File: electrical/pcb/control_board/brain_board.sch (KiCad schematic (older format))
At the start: 7 parts, among them J10 6posheader, J27 PPTC102LFBN-RC, J6 S9175-ND_rpi_breakout, J7 S9175-ND_rpi_breakout, J8 6posheader

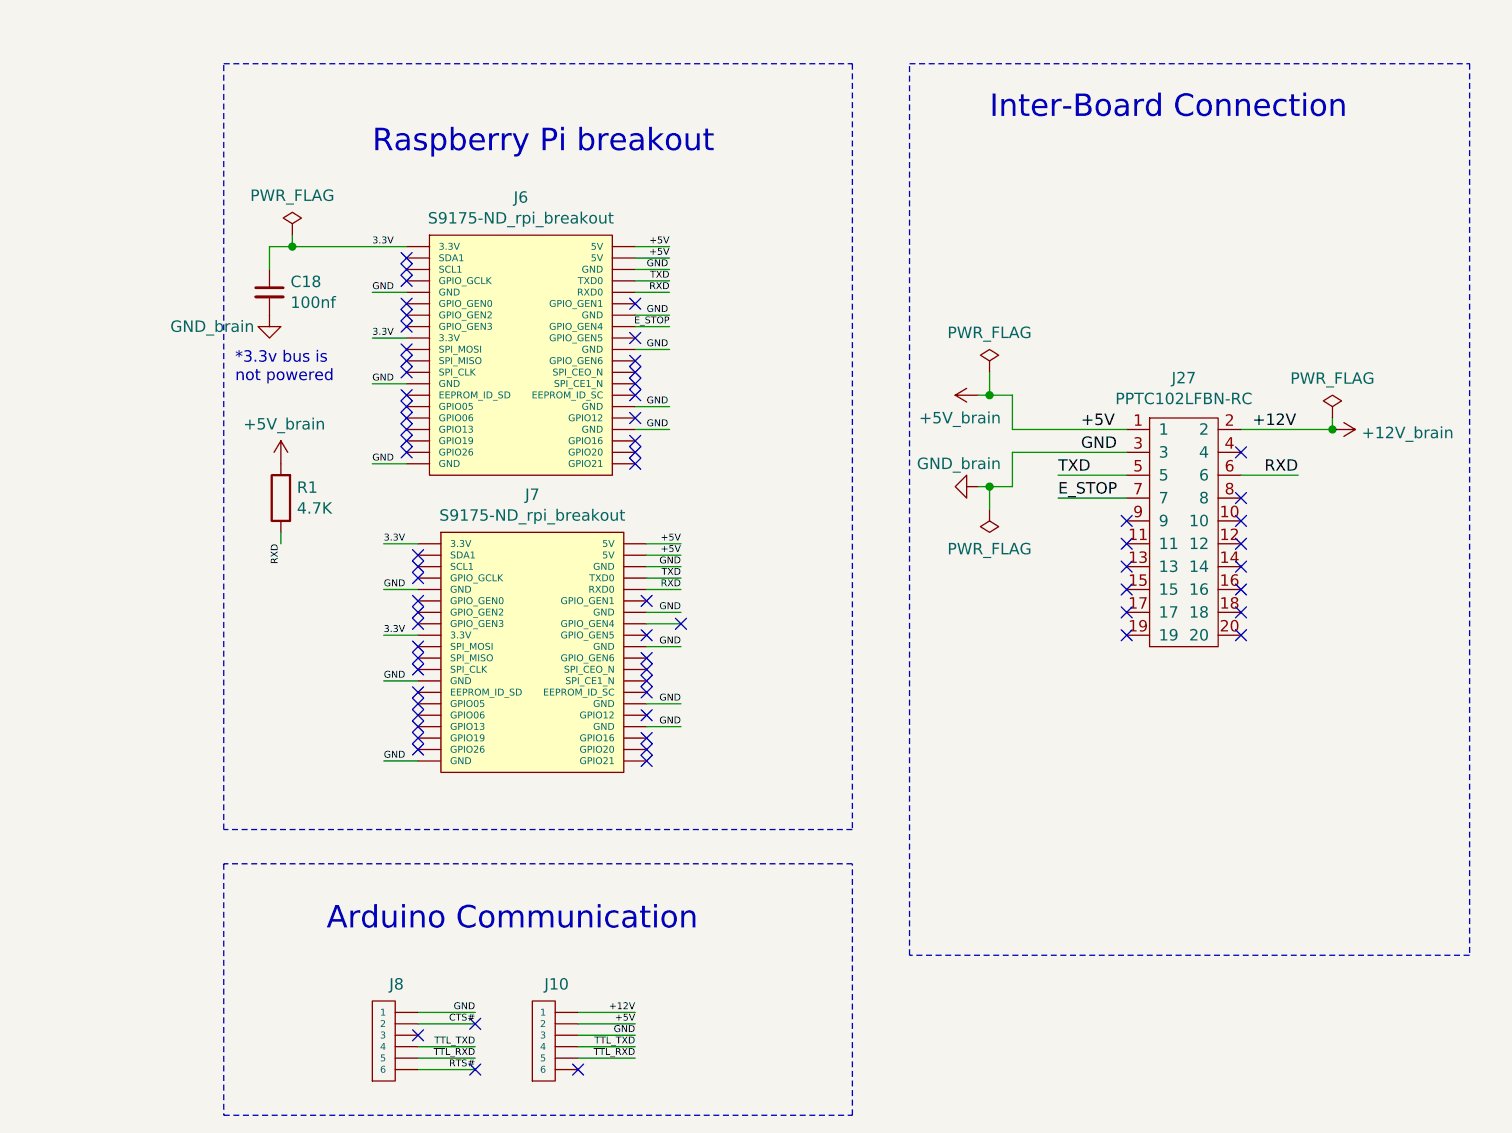
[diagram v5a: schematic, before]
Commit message: Adding secondary e-stop line connected to s4 on roboclaw, along with a 2 pin header for it on the brain board
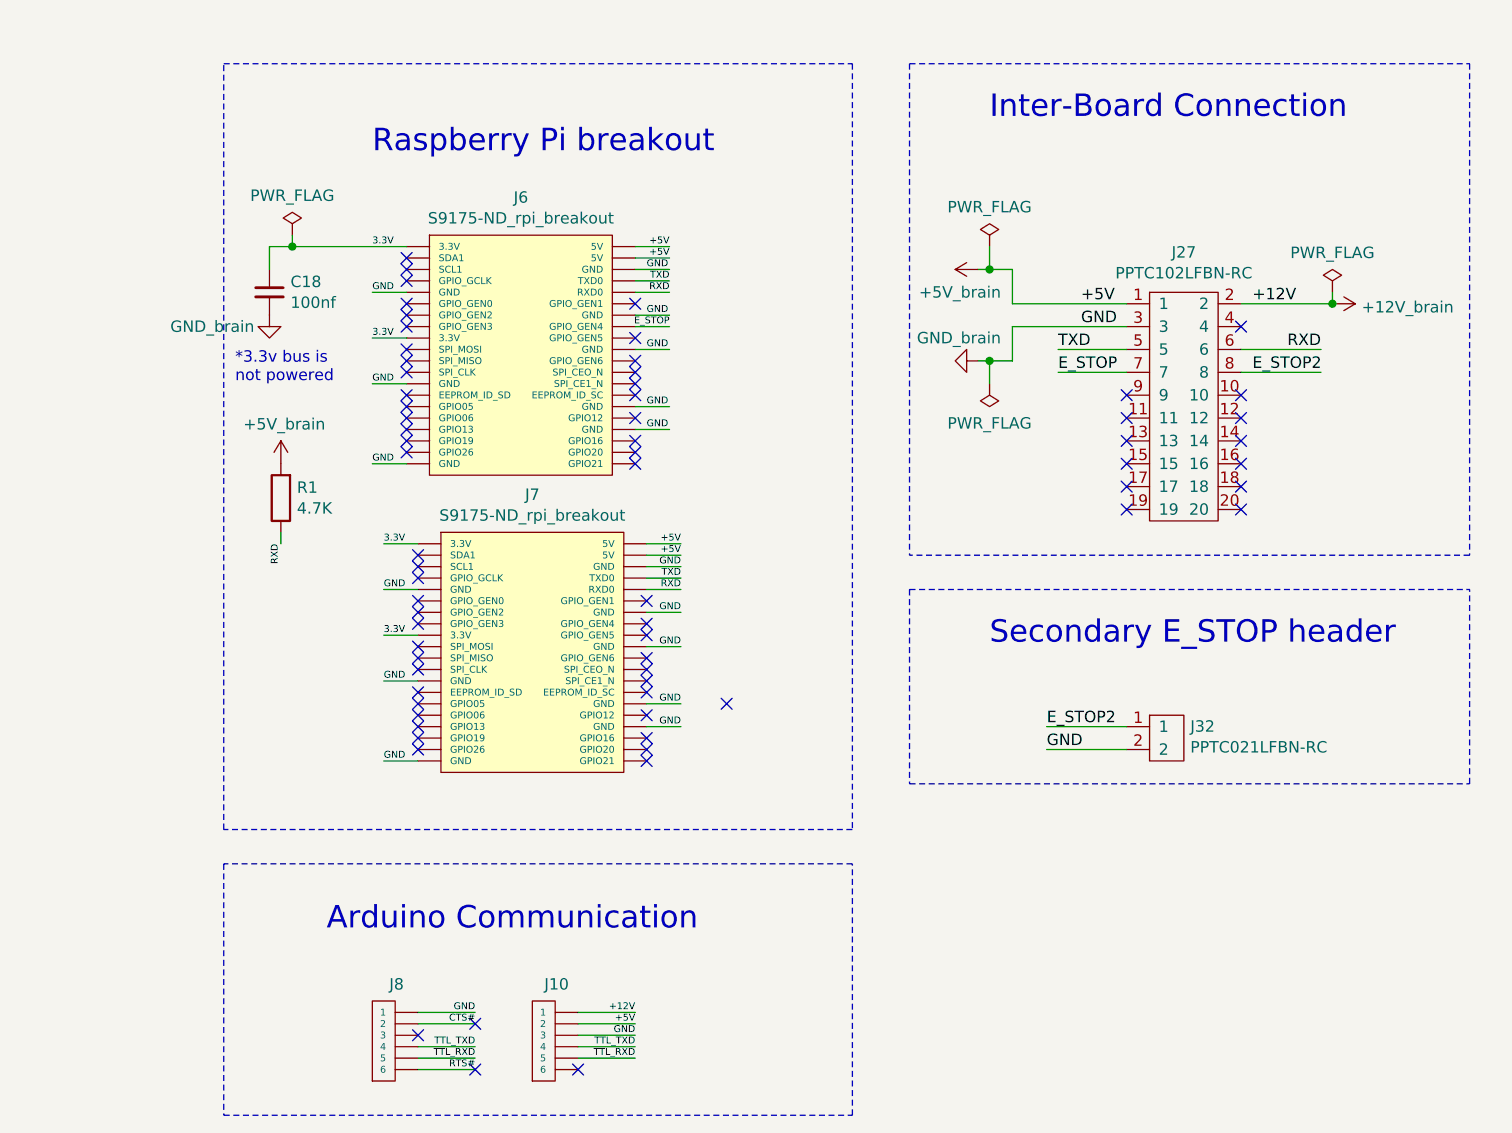
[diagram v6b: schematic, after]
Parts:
- added J32: PPTC021LFBN-RC, JPL Robotics:PPTC021LFBN-RC, symbol JPL_Robotics_Lib:PPTC021LFBN-RC
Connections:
- net labels added: E_STOP2
- wire segments 59 -> 61
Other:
- note added: "Secondary E_STOP header"
- moved on the sheet: J27
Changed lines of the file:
@@
 Wire Wire Line
 	4550 5700 4800 5700
-Wire Wire Line
-	5000 3850 4850 3850
 NoConn ~ 4550 5800
 NoConn ~ 4100 5800
 NoConn ~ 4100 5600
-NoConn ~ 5000 3850
 NoConn ~ 3800 2650
 NoConn ~ 3800 2750
@@
 NoConn ~ 3850 3600
 Wire Notes Line style solid rgb(0, 0, 0)
-	8450 1400 8450 5300
-Wire Notes Line style solid rgb(0, 0, 0)
-	8450 5300 6000 5300
-Wire Notes Line style solid rgb(0, 0, 0)
-	6000 5300 6000 1400
-Wire Notes Line style solid rgb(0, 0, 0)
 	6000 1400 8450 1400
 Text Notes 6350 1650 0    98   ~ 0
 Inter-Board Connection
-Text Label 6650 3200 0    50   ~ 0
+Text Label 6650 2650 0    50   ~ 0
 TXD
-Text Label 7700 3200 2    50   ~ 0
+Text Label 7800 2650 2    50   ~ 0
 RXD
-Text Label 6650 3300 0    50   ~ 0
+Text Label 6650 2750 0    50   ~ 0
 E_STOP
 Wire Wire Line
-	6650 3200 6950 3200
-Wire Wire Line
-	6650 3300 6950 3300
-Wire Wire Line
-	7450 3200 7700 3200
+	6650 2650 6950 2650
+Wire Wire Line
+	6650 2750 6950 2750
 $Comp
 L JPL_Robotics_Lib:PPTC102LFBN-RC J27
 U 1 1 60EE139B
-P 7200 2850
-F 0 "J27" H 7200 2925 50  0000 C CNN
-F 1 "PPTC102LFBN-RC" H 7200 2834 50  0000 C CNN
-F 2 "JPL Robotics:PPTC102LFBN-RC" H 7500 2850 50  0001 C CNN
-F 3 "" H 7500 2850 50  0001 C CNN
-	1    7200 2850
-	1    0    0    -1
-$EndComp
-NoConn ~ 7450 3300
-NoConn ~ 7450 3400
-NoConn ~ 7450 3500
-NoConn ~ 7450 3600
-NoConn ~ 7450 3700
-NoConn ~ 7450 3800
-NoConn ~ 7450 3900
-NoConn ~ 6950 3400
-NoConn ~ 6950 3500
-NoConn ~ 6950 3600
-NoConn ~ 6950 3700
-NoConn ~ 6950 3800
-NoConn ~ 6950 3900
+P 7200 2300
+F 0 "J27" H 7200 2375 50  0000 C CNN
+F 1 "PPTC102LFBN-RC" H 7200 2284 50  0000 C CNN
+F 2 "JPL Robotics:PPTC102LFBN-RC" H 7500 2300 50  0001 C CNN
+F 3 "" H 7500 2300 50  0001 C CNN
+	1    7200 2300
+	1    0    0    -1
+$EndComp
+NoConn ~ 7450 2850
+NoConn ~ 7450 2950
+NoConn ~ 7450 3050
+NoConn ~ 7450 3150
+NoConn ~ 7450 3250
+NoConn ~ 7450 3350
+NoConn ~ 6950 2850
+NoConn ~ 6950 2950
+NoConn ~ 6950 3050
+NoConn ~ 6950 3150
+NoConn ~ 6950 3250
+NoConn ~ 6950 3350
 $Comp
 L JPL_Robotics_Lib:+5V_brain #PWR0144
@@
 L JPL_Robotics_Lib:+5V_brain #PWR0146
 U 1 1 618ECDE5
-P 6300 2850
-F 0 "#PWR0146" H 6300 2700 50  0001 C CNN
-F 1 "+5V_brain" V 6200 2750 50  0000 L CNN
-F 2 "" H 6300 2850 50  0001 C CNN
-F 3 "" H 6300 2850 50  0001 C CNN
-	1    6300 2850
+P 6300 2300
+F 0 "#PWR0146" H 6300 2150 50  0001 C CNN
+F 1 "+5V_brain" V 6200 2200 50  0000 L CNN
+F 2 "" H 6300 2300 50  0001 C CNN
+F 3 "" H 6300 2300 50  0001 C CNN
+	1    6300 2300
 	0    -1   -1   0
 $EndComp
@@
 L JPL_Robotics_Lib:GND_brain #PWR0147
 U 1 1 618EE99B
-P 6300 3250
-F 0 "#PWR0147" H 6300 3000 50  0001 C CNN
-F 1 "GND_brain" V 6200 3350 50  0000 R CNN
-F 2 "" H 6300 3250 50  0001 C CNN
-F 3 "" H 6300 3250 50  0001 C CNN
-	1    6300 3250
+P 6300 2700
+F 0 "#PWR0147" H 6300 2450 50  0001 C CNN
+F 1 "GND_brain" V 6200 2800 50  0000 R CNN
+F 2 "" H 6300 2700 50  0001 C CNN
+F 3 "" H 6300 2700 50  0001 C CNN
+	1    6300 2700
 	0    1    1    0
 $EndComp
@@
 L JPL_Robotics_Lib:+12V_brain #PWR0148
 U 1 1 618F0639
-P 7850 3000
-F 0 "#PWR0148" H 7850 2850 50  0001 C CNN
-F 1 "+12V_brain" V 7865 3128 50  0000 L CNN
-F 2 "" H 7850 3000 50  0001 C CNN
-F 3 "" H 7850 3000 50  0001 C CNN
-	1    7850 3000
+P 7850 2450
+F 0 "#PWR0148" H 7850 2300 50  0001 C CNN
+F 1 "+12V_brain" V 7865 2578 50  0000 L CNN
+F 2 "" H 7850 2450 50  0001 C CNN
+F 3 "" H 7850 2450 50  0001 C CNN
+	1    7850 2450
 	0    1    1    0
 $EndComp
-Text Label 6750 3000 0    50   ~ 0
+Text Label 6750 2450 0    50   ~ 0
 +5V
-Text Label 6750 3100 0    50   ~ 0
+Text Label 6750 2550 0    50   ~ 0
 GND
-Text Label 7500 3000 0    50   ~ 0
+Text Label 7500 2450 0    50   ~ 0
 +12V
-NoConn ~ 7450 3100
+NoConn ~ 7450 2550
 $Comp
 L power:PWR_FLAG #FLG0101
 U 1 1 6195B322
-P 6350 2750
-F 0 "#FLG0101" H 6350 2825 50  0001 C CNN
-F 1 "PWR_FLAG" H 6350 2923 50  0000 C CNN
-F 2 "" H 6350 2750 50  0001 C CNN
-F 3 "~" H 6350 2750 50  0001 C CNN
-	1    6350 2750
+P 6350 2200
+F 0 "#FLG0101" H 6350 2275 50  0001 C CNN
+F 1 "PWR_FLAG" H 6350 2373 50  0000 C CNN
+F 2 "" H 6350 2200 50  0001 C CNN
+F 3 "~" H 6350 2200 50  0001 C CNN
+	1    6350 2200
 	1    0    0    -1
 $EndComp
@@
 L power:PWR_FLAG #FLG0102
 U 1 1 6195CC58
-P 6350 3350
-F 0 "#FLG0102" H 6350 3425 50  0001 C CNN
-F 1 "PWR_FLAG" H 6350 3523 50  0000 C CNN
-F 2 "" H 6350 3350 50  0001 C CNN
-F 3 "~" H 6350 3350 50  0001 C CNN
-	1    6350 3350
+P 6350 2800
+F 0 "#FLG0102" H 6350 2875 50  0001 C CNN
+F 1 "PWR_FLAG" H 6350 2973 50  0000 C CNN
+F 2 "" H 6350 2800 50  0001 C CNN
+F 3 "~" H 6350 2800 50  0001 C CNN
+	1    6350 2800
 	-1   0    0    1
 $EndComp
 Wire Wire Line
-	6450 3250 6350 3250
-Wire Wire Line
-	6450 3100 6950 3100
-Wire Wire Line
-	6350 3250 6350 3350
-Connection ~ 6350 3250
-Wire Wire Line
-	6350 3250 6300 3250
-Wire Wire Line
-	6450 2850 6350 2850
-Wire Wire Line
-	6450 3000 6950 3000
-Wire Wire Line
-	6350 2850 6350 2750
-Connection ~ 6350 2850
-Wire Wire Line
-	6350 2850 6300 2850
-Wire Wire Line
-	6450 3100 6450 3250
-Wire Wire Line
-	6450 2850 6450 3000
-Wire Wire Line
-	7450 3000 7850 3000
+	6450 2700 6350 2700
+Wire Wire Line
+	6450 2550 6950 2550
+Wire Wire Line
+	6350 2700 6350 2800
+Connection ~ 6350 2700
+Wire Wire Line
+	6350 2700 6300 2700
+Wire Wire Line
+	6450 2300 6350 2300
+Wire Wire Line
+	6450 2450 6950 2450
+Wire Wire Line
+	6350 2300 6350 2200
+Connection ~ 6350 2300
+Wire Wire Line
+	6350 2300 6300 2300
+Wire Wire Line
+	6450 2550 6450 2700
+Wire Wire Line
+	6450 2300 6450 2450
+Wire Wire Line
+	7450 2450 7850 2450
 $Comp
 L power:PWR_FLAG #FLG0103
 U 1 1 619765A5
-P 7850 2950
-F 0 "#FLG0103" H 7850 3025 50  0001 C CNN
-F 1 "PWR_FLAG" H 7850 3123 50  0000 C CNN
-F 2 "" H 7850 2950 50  0001 C CNN
-F 3 "~" H 7850 2950 50  0001 C CNN
-	1    7850 2950
-	1    0    0    -1
-$EndComp
-Wire Wire Line
-	7850 2950 7850 3000
-Connection ~ 7850 3000
+P 7850 2400
+F 0 "#FLG0103" H 7850 2475 50  0001 C CNN
+F 1 "PWR_FLAG" H 7850 2573 50  0000 C CNN
+F 2 "" H 7850 2400 50  0001 C CNN
+F 3 "~" H 7850 2400 50  0001 C CNN
+	1    7850 2400
+	1    0    0    -1
+$EndComp
+Wire Wire Line
+	7850 2400 7850 2450
+Connection ~ 7850 2450
+NoConn ~ 4850 3850
+NoConn ~ 5200 4200
+Wire Notes Line
+	6000 1400 6000 3550
+Wire Notes Line
+	8450 1400 8450 3550
+Wire Notes Line
+	8450 3550 6000 3550
+Wire Notes Line style solid rgb(0, 0, 0)
+	6000 3700 8450 3700
+Text Notes 6350 3950 0    98   ~ 0
+Secondary E_STOP header
+$Comp
+L JPL_Robotics_Lib:PPTC021LFBN-RC J32
+U 1 1 609D84ED
+P 7200 4150
+F 0 "J32" H 7228 4001 50  0000 L CNN
+F 1 "PPTC021LFBN-RC" H 7228 3910 50  0000 L CNN
+F 2 "JPL Robotics:PPTC021LFBN-RC" H 7500 4150 50  0001 C CNN
+F 3 "" H 7500 4150 50  0001 C CNN
+	1    7200 4150
+	1    0    0    -1
+$EndComp
+Wire Wire Line
+	7450 2750 7800 2750
+Text Label 7500 2750 0    50   ~ 0
+E_STOP2
+Wire Wire Line
+	7450 2650 7800 2650
+Wire Wire Line
+	6600 4400 6950 4400
+Wire Wire Line
+	6600 4300 6950 4300
+Text Label 6600 4300 0    50   ~ 0
+E_STOP2
+Text Label 6600 4400 0    50   ~ 0
+GND
+Wire Notes Line
+	6000 3700 6000 4550
+Wire Notes Line
+	6000 4550 8450 4550
+Wire Notes Line
+	8450 4550 8450 3700
 $EndSCHEMATC

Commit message: Adding headers and rpi connections for gst
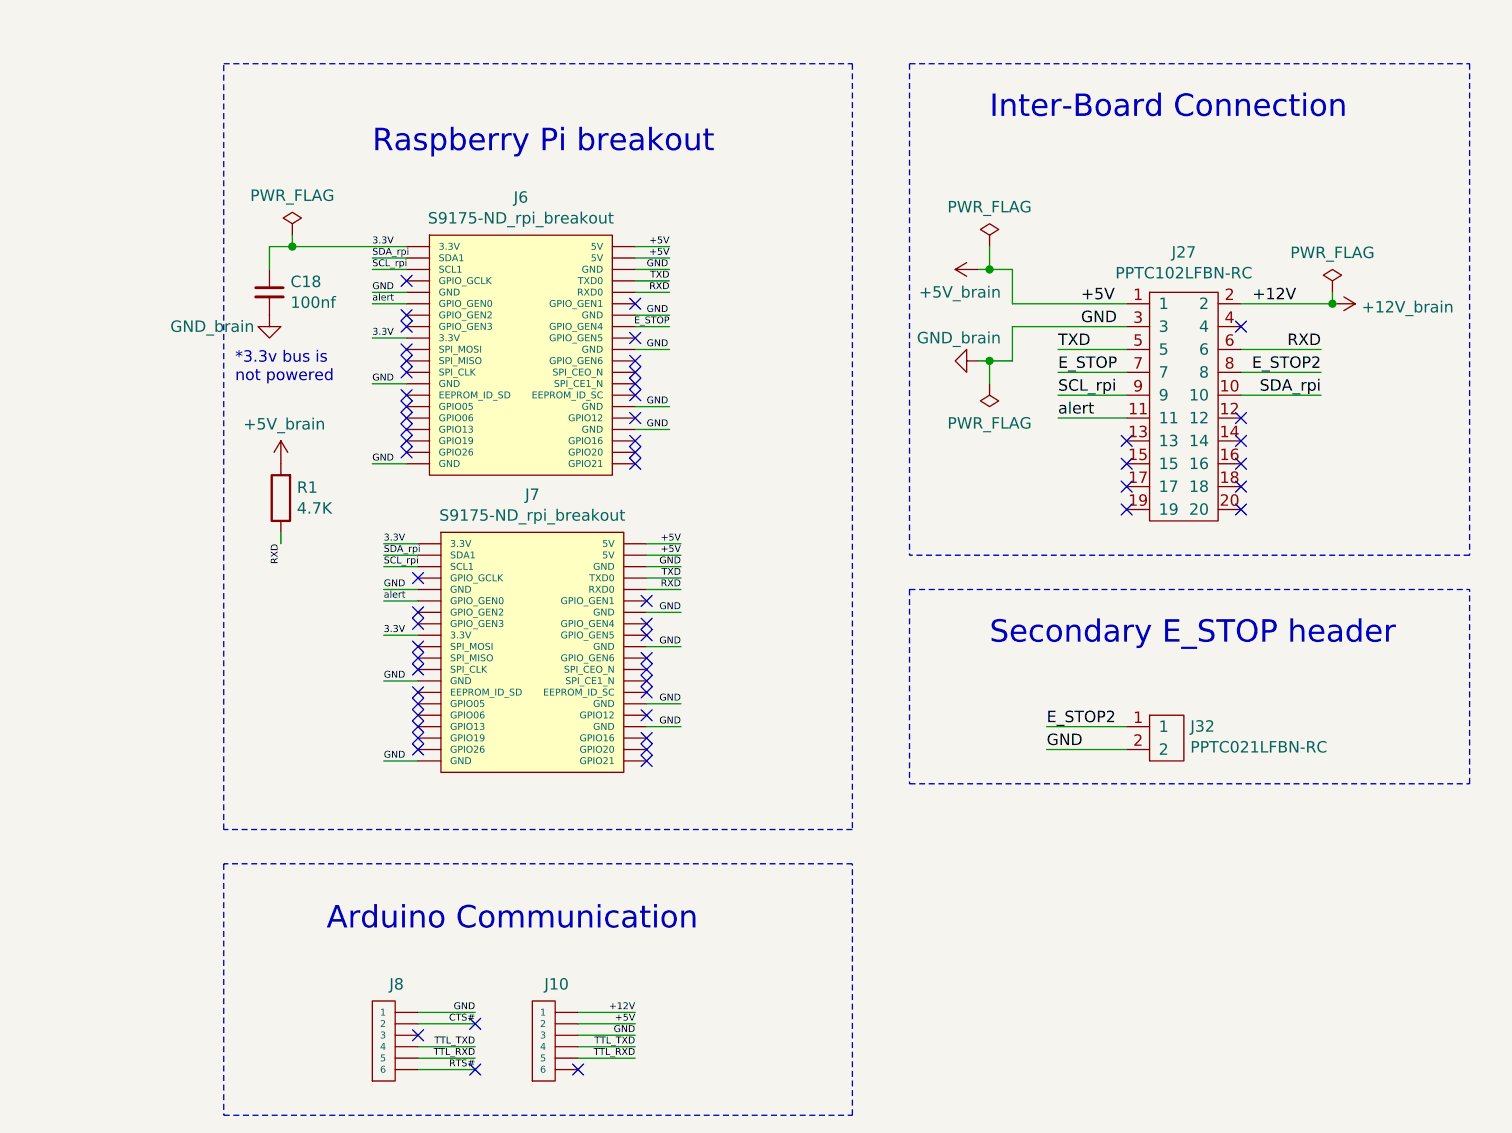
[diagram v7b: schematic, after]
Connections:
- net labels added: SCL_rpi, SDA_rpi, alert
- wire segments 61 -> 70
- no-connect marks 69 -> 59
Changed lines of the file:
@@
 $EndComp
 NoConn ~ 3800 2350
-NoConn ~ 3800 2450
 NoConn ~ 3800 2500
 NoConn ~ 3800 2550
@@
 NoConn ~ 4800 2450
 NoConn ~ 3850 3650
-NoConn ~ 3850 3750
 NoConn ~ 3850 3800
 NoConn ~ 3850 3850
@@
 NoConn ~ 4850 3900
 NoConn ~ 4850 3750
-NoConn ~ 3800 2250
-NoConn ~ 3800 2300
-NoConn ~ 3850 3550
-NoConn ~ 3850 3600
 Wire Notes Line style solid rgb(0, 0, 0)
 	6000 1400 8450 1400
@@
 	1    0    0    -1
 $EndComp
-NoConn ~ 7450 2850
 NoConn ~ 7450 2950
 NoConn ~ 7450 3050
@@
 NoConn ~ 7450 3250
 NoConn ~ 7450 3350
-NoConn ~ 6950 2850
-NoConn ~ 6950 2950
 NoConn ~ 6950 3050
 NoConn ~ 6950 3150
@@
 Connection ~ 7850 2450
 NoConn ~ 4850 3850
-NoConn ~ 5200 4200
 Wire Notes Line
 	6000 1400 6000 3550
@@
 Wire Wire Line
 	7450 2750 7800 2750
-Text Label 7500 2750 0    50   ~ 0
+Text Label 7800 2750 2    50   ~ 0
 E_STOP2
 Wire Wire Line
@@
 Wire Notes Line
 	8450 4550 8450 3700
+Wire Wire Line
+	3800 2450 3650 2450
+Text Label 3650 2450 0    30   ~ 0
+alert
+Wire Wire Line
+	6950 2950 6650 2950
+Text Label 6650 2950 0    50   ~ 0
+alert
+Wire Wire Line
+	6950 2850 6650 2850
+Text Label 6650 2850 0    50   ~ 0
+SCL_rpi
+Wire Wire Line
+	7450 2850 7800 2850
+Text Label 7800 2850 2    50   ~ 0
+SDA_rpi
+Wire Wire Line
+	3800 2250 3650 2250
+Wire Wire Line
+	3800 2300 3650 2300
+Text Label 3650 2250 0    30   ~ 0
+SDA_rpi
+Text Label 3650 2300 0    30   ~ 0
+SCL_rpi
+Wire Wire Line
+	3850 3550 3700 3550
+Wire Wire Line
+	3850 3600 3700 3600
+Text Label 3700 3550 0    30   ~ 0
+SDA_rpi
+Text Label 3700 3600 0    30   ~ 0
+SCL_rpi
+Wire Wire Line
+	3850 3750 3700 3750
+Text Label 3700 3750 0    30   ~ 0
+alert
 $EndSCHEMATC
